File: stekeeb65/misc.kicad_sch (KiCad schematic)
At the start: 7 parts, among them J0 Conn_02x03_Odd_Even, J1 TYPE-C-31-M12_13_EDITED, U0 WE-TVS-82400102

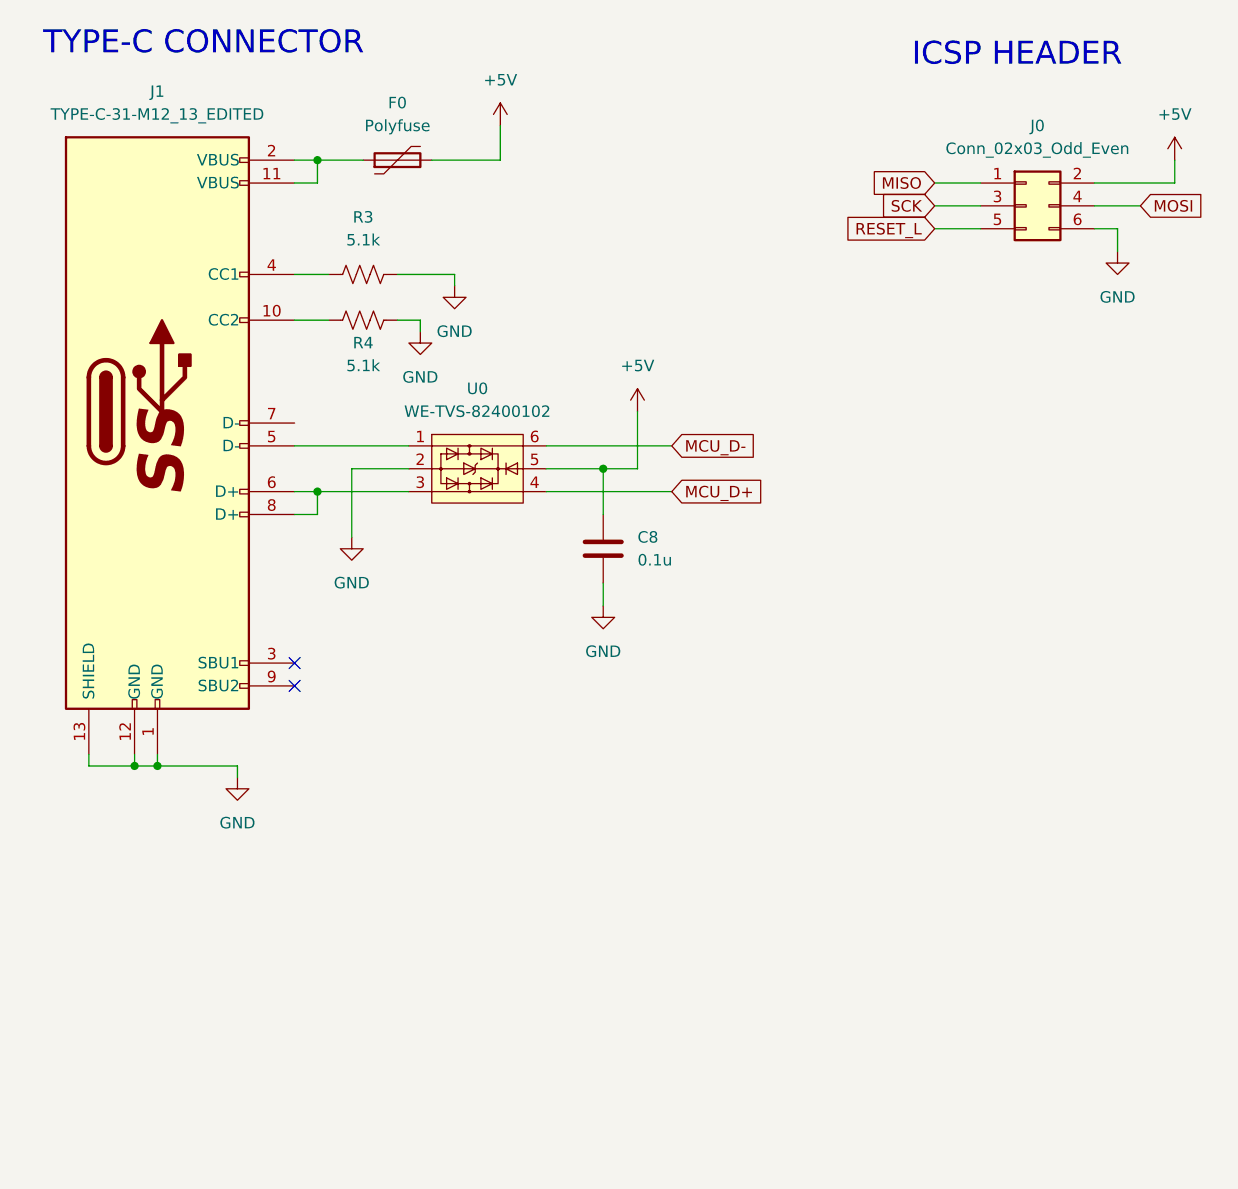
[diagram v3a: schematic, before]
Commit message: Started layout for keyboard. still need to verify LED driver schematic
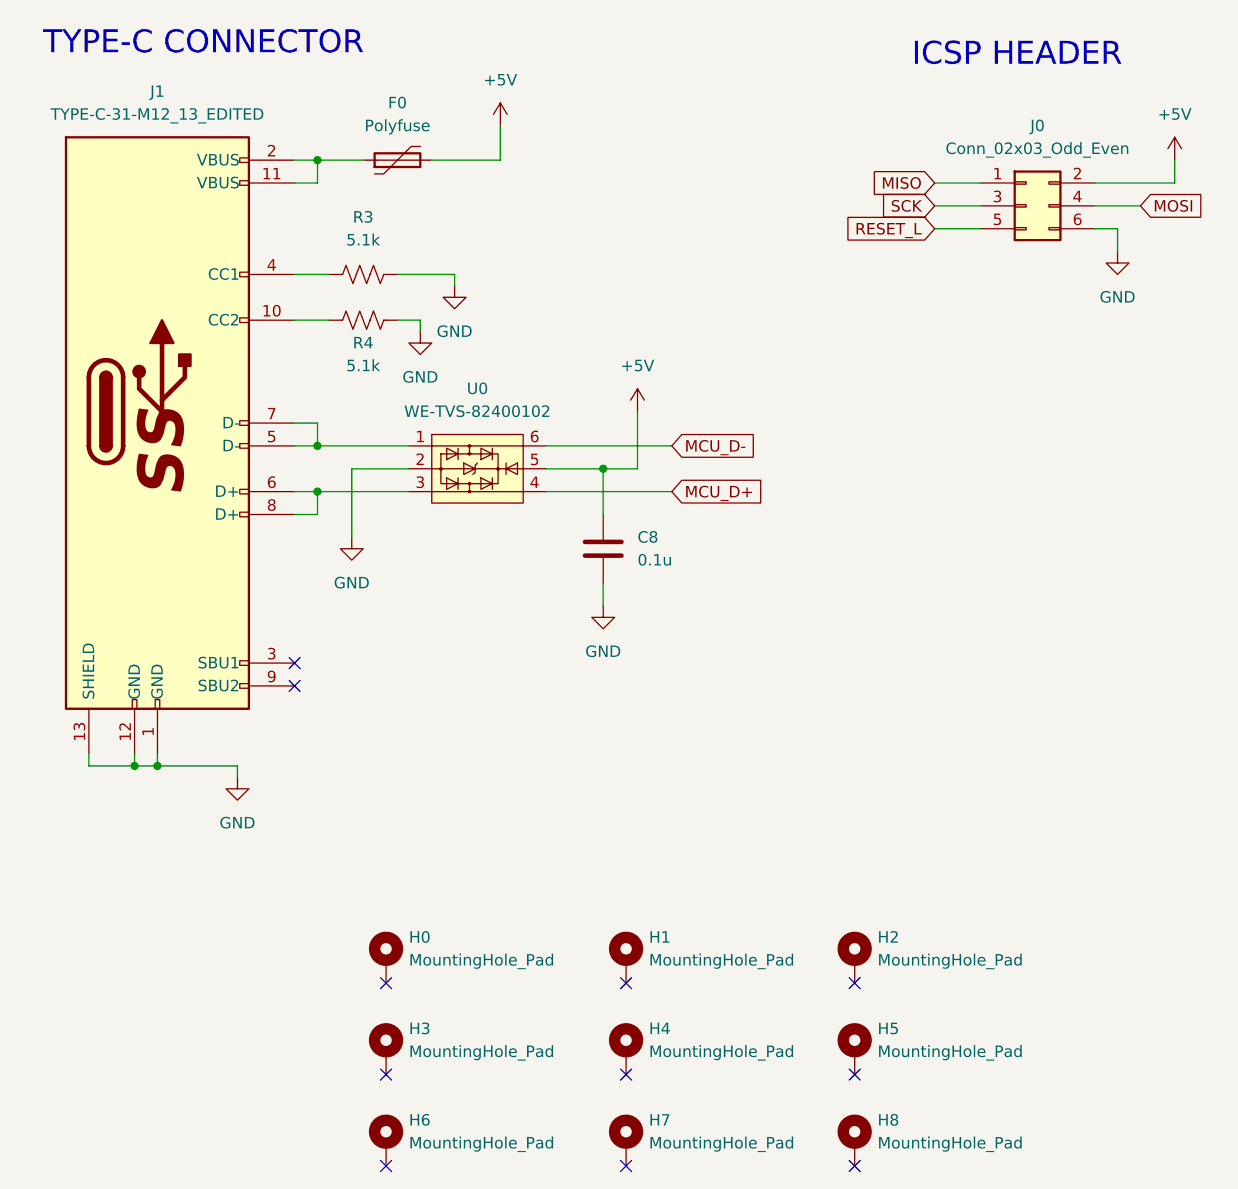
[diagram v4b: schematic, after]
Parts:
- added H0, H1, H2, H3, H4, H5, H6, H7, H8: MountingHole_Pad, MountingHole:MountingHole_2.2mm_M2_DIN965_Pad_TopOnly, symbol Mechanical:MountingHole_Pad
- C8: footprint Capacitor_SMD:C_0805_2012Metric_Pad1.18x1.45mm_HandSolder -> Capacitor_SMD:C_0603_1608Metric_Pad1.08x0.95mm_HandSolder
- J1: footprint Type-C:HRO-TYPE-C-31-M-12-HandSoldering -> Type-C:HRO-TYPE-C-31-M-12-Assembly
- R3, R4: footprint Resistor_SMD:R_0805_2012Metric_Pad1.20x1.40mm_HandSolder -> Resistor_SMD:R_0603_1608Metric_Pad0.98x0.95mm_HandSolder
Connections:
- net at J1.5 (D-), U0.1: now also J1.7 (D-)
- no-connect marks 2 -> 11
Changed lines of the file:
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@@
   (junction (at 57.15 71.12) (diameter 0) (color 0 0 0 0)
   )
+  (junction (at 57.15 66.04) (diameter 0) (color 0 0 0 0)
+  )
   (junction (at 88.9 68.58) (diameter 0) (color 0 0 0 0)
   )
@@
   (junction (at 57.15 34.29) (diameter 0) (color 0 0 0 0)
   )
+  (no_connect (at 91.44 135.89))
+  (no_connect (at 91.44 146.05))
+  (no_connect (at 116.84 135.89))
+  (no_connect (at 116.84 125.73))
+  (no_connect (at 64.77 125.73))
+  (no_connect (at 91.44 125.73))
+  (no_connect (at 64.77 146.05))
+  (no_connect (at 116.84 146.05))
   (no_connect (at 54.61 92.71))
   (no_connect (at 54.61 90.17))
+  (no_connect (at 64.77 135.89))
   (wire (pts (xy 31.75 101.6) (xy 31.75 100.33))
     (stroke (width 0) (type default) (color 0 0 0 0))
@@
     (stroke (width 0) (type default) (color 0 0 0 0))
   )
+  (wire (pts (xy 54.61 63.5) (xy 57.15 63.5))
+    (stroke (width 0) (type default) (color 0 0 0 0))
+  )
   (wire (pts (xy 66.04 46.99) (xy 72.39 46.99))
     (stroke (width 0) (type default) (color 0 0 0 0))
@@
     (stroke (width 0) (type default) (color 0 0 0 0))
   )
+  (wire (pts (xy 57.15 63.5) (xy 57.15 66.04))
+    (stroke (width 0) (type default) (color 0 0 0 0))
+  )
   (wire (pts (xy 146.05 41.91) (xy 146.05 44.45))
     (stroke (width 0) (type default) (color 0 0 0 0))
@@
     (stroke (width 0) (type default) (color 0 0 0 0))
   )
-  (wire (pts (xy 54.61 66.04) (xy 67.31 66.04))
+  (wire (pts (xy 54.61 66.04) (xy 57.15 66.04))
     (stroke (width 0) (type default) (color 0 0 0 0))
   )
   (wire (pts (xy 60.96 76.2) (xy 60.96 68.58))
+    (stroke (width 0) (type default) (color 0 0 0 0))
+  )
+  (wire (pts (xy 57.15 66.04) (xy 67.31 66.04))
     (stroke (width 0) (type default) (color 0 0 0 0))
   )
@@
     (pin "1")
   )
+  (symbol (lib_id "Mechanical:MountingHole_Pad") (at 116.84 133.35 0) (unit 1)
+    (in_bom yes) (on_board yes) (fields_autoplaced)
+    (property "Reference" "H5" (id 0) (at 119.38 130.8099 0)
+      (effects (font (size 1.27 1.27)) (justify left))
+    )
+    (property "Value" "MountingHole_Pad" (id 1) (at 119.38 133.3499 0)
+      (effects (font (size 1.27 1.27)) (justify left))
+    )
+    (property "Footprint" "MountingHole:MountingHole_2.2mm_M2_DIN965_Pad_TopOnly" (id 2) (at 116.84 133.35 0)
+      (effects (font (size 1.27 1.27)) hide)
+    )
+    (property "Datasheet" "~" (id 3) (at 116.84 133.35 0)
+      (effects (font (size 1.27 1.27)) hide)
+    )
+    (pin "1")
+  )
+  (symbol (lib_id "Mechanical:MountingHole_Pad") (at 64.77 123.19 0) (unit 1)
+    (in_bom yes) (on_board yes) (fields_autoplaced)
+    (property "Reference" "H0" (id 0) (at 67.31 120.6499 0)
+      (effects (font (size 1.27 1.27)) (justify left))
+    )
+    (property "Value" "MountingHole_Pad" (id 1) (at 67.31 123.1899 0)
+      (effects (font (size 1.27 1.27)) (justify left))
+    )
+    (property "Footprint" "MountingHole:MountingHole_2.2mm_M2_DIN965_Pad_TopOnly" (id 2) (at 64.77 123.19 0)
+      (effects (font (size 1.27 1.27)) hide)
+    )
+    (property "Datasheet" "~" (id 3) (at 64.77 123.19 0)
+      (effects (font (size 1.27 1.27)) hide)
+    )
+    (pin "1")
+  )
   (symbol (lib_id "Device:C") (at 88.9 77.47 0) (unit 1)
     (in_bom yes) (on_board yes) (fields_autoplaced)
@@
       (effects (font (size 1.27 1.27)) (justify left))
     )
-    (property "Footprint" "Capacitor_SMD:C_0805_2012Metric_Pad1.18x1.45mm_HandSolder" (id 2) (at 89.8652 81.28 0)
+    (property "Footprint" "Capacitor_SMD:C_0603_1608Metric_Pad1.08x0.95mm_HandSolder" (id 2) (at 89.8652 81.28 0)
       (effects (font (size 1.27 1.27)) hide)
     )
@@
     (property "Reference" "J1" (id 0) (at 39.37 26.67 0))
     (property "Value" "TYPE-C-31-M12_13_EDITED" (id 1) (at 39.37 29.21 0))
-    (property "Footprint" "Type-C:HRO-TYPE-C-31-M-12-HandSoldering" (id 2) (at 26.67 62.23 90)
+    (property "Footprint" "Type-C:HRO-TYPE-C-31-M-12-Assembly" (id 2) (at 26.67 62.23 90)
       (effects (font (size 1.27 1.27)) hide)
     )
@@
     (property "Reference" "R3" (id 0) (at 62.23 40.64 90))
     (property "Value" "5.1k" (id 1) (at 62.23 43.18 90))
-    (property "Footprint" "Resistor_SMD:R_0805_2012Metric_Pad1.20x1.40mm_HandSolder" (id 2) (at 62.484 45.974 90)
+    (property "Footprint" "Resistor_SMD:R_0603_1608Metric_Pad0.98x0.95mm_HandSolder" (id 2) (at 62.484 45.974 90)
       (effects (font (size 1.27 1.27)) hide)
     )
@@
     (pin "1")
     (pin "2")
+  )
+  (symbol (lib_id "Mechanical:MountingHole_Pad") (at 91.44 123.19 0) (unit 1)
+    (in_bom yes) (on_board yes) (fields_autoplaced)
+    (property "Reference" "H1" (id 0) (at 93.98 120.6499 0)
+      (effects (font (size 1.27 1.27)) (justify left))
+    )
+    (property "Value" "MountingHole_Pad" (id 1) (at 93.98 123.1899 0)
+      (effects (font (size 1.27 1.27)) (justify left))
+    )
+    (property "Footprint" "MountingHole:MountingHole_2.2mm_M2_DIN965_Pad_TopOnly" (id 2) (at 91.44 123.19 0)
+      (effects (font (size 1.27 1.27)) hide)
+    )
+    (property "Datasheet" "~" (id 3) (at 91.44 123.19 0)
+      (effects (font (size 1.27 1.27)) hide)
+    )
+    (pin "1")
   )
   (symbol (lib_id "power:+5V") (at 92.71 62.23 0) (unit 1)
@@
     (property "Reference" "R4" (id 0) (at 62.23 54.61 90))
     (property "Value" "5.1k" (id 1) (at 62.23 57.15 90))
-    (property "Footprint" "Resistor_SMD:R_0805_2012Metric_Pad1.20x1.40mm_HandSolder" (id 2) (at 62.484 51.054 90)
+    (property "Footprint" "Resistor_SMD:R_0603_1608Metric_Pad0.98x0.95mm_HandSolder" (id 2) (at 62.484 51.054 90)
       (effects (font (size 1.27 1.27)) hide)
     )
@@
     (pin "1")
   )
+  (symbol (lib_id "Mechanical:MountingHole_Pad") (at 91.44 133.35 0) (unit 1)
+    (in_bom yes) (on_board yes) (fields_autoplaced)
+    (property "Reference" "H4" (id 0) (at 93.98 130.8099 0)
+      (effects (font (size 1.27 1.27)) (justify left))
+    )
+    (property "Value" "MountingHole_Pad" (id 1) (at 93.98 133.3499 0)
+      (effects (font (size 1.27 1.27)) (justify left))
+    )
+    (property "Footprint" "MountingHole:MountingHole_2.2mm_M2_DIN965_Pad_TopOnly" (id 2) (at 91.44 133.35 0)
+      (effects (font (size 1.27 1.27)) hide)
+    )
+    (property "Datasheet" "~" (id 3) (at 91.44 133.35 0)
+      (effects (font (size 1.27 1.27)) hide)
+    )
+    (pin "1")
+  )
   (symbol (lib_id "power:+5V") (at 77.47 30.48 0) (unit 1)
     (in_bom yes) (on_board yes) (fields_autoplaced)
@@
       (effects (font (size 1.27 1.27)) hide)
     )
+    (pin "1")
+  )
+  (symbol (lib_id "Mechanical:MountingHole_Pad") (at 64.77 133.35 0) (unit 1)
+    (in_bom yes) (on_board yes) (fields_autoplaced)
+    (property "Reference" "H3" (id 0) (at 67.31 130.8099 0)
+      (effects (font (size 1.27 1.27)) (justify left))
+    )
+    (property "Value" "MountingHole_Pad" (id 1) (at 67.31 133.3499 0)
+      (effects (font (size 1.27 1.27)) (justify left))
+    )
+    (property "Footprint" "MountingHole:MountingHole_2.2mm_M2_DIN965_Pad_TopOnly" (id 2) (at 64.77 133.35 0)
+      (effects (font (size 1.27 1.27)) hide)
+    )
+    (property "Datasheet" "~" (id 3) (at 64.77 133.35 0)
+      (effects (font (size 1.27 1.27)) hide)
+    )
+    (pin "1")
+  )
+  (symbol (lib_id "Mechanical:MountingHole_Pad") (at 91.44 143.51 0) (unit 1)
+    (in_bom yes) (on_board yes) (fields_autoplaced)
+    (property "Reference" "H7" (id 0) (at 93.98 140.9699 0)
+      (effects (font (size 1.27 1.27)) (justify left))
+    )
+    (property "Value" "MountingHole_Pad" (id 1) (at 93.98 143.5099 0)
+      (effects (font (size 1.27 1.27)) (justify left))
+    )
+    (property "Footprint" "MountingHole:MountingHole_2.2mm_M2_DIN965_Pad_TopOnly" (id 2) (at 91.44 143.51 0)
+      (effects (font (size 1.27 1.27)) hide)
+    )
+    (property "Datasheet" "~" (id 3) (at 91.44 143.51 0)
+      (effects (font (size 1.27 1.27)) hide)
+    )
+    (pin "1")
+  )
+  (symbol (lib_id "Mechanical:MountingHole_Pad") (at 116.84 143.51 0) (unit 1)
+    (in_bom yes) (on_board yes) (fields_autoplaced)
+    (property "Reference" "H8" (id 0) (at 119.38 140.9699 0)
+      (effects (font (size 1.27 1.27)) (justify left))
+    )
+    (property "Value" "MountingHole_Pad" (id 1) (at 119.38 143.5099 0)
+      (effects (font (size 1.27 1.27)) (justify left))
+    )
+    (property "Footprint" "MountingHole:MountingHole_2.2mm_M2_DIN965_Pad_TopOnly" (id 2) (at 116.84 143.51 0)
+      (effects (font (size 1.27 1.27)) hide)
+    )
+    (property "Datasheet" "~" (id 3) (at 116.84 143.51 0)
+      (effects (font (size 1.27 1.27)) hide)
+    )
+    (pin "1")
+  )
+  (symbol (lib_id "Mechanical:MountingHole_Pad") (at 64.77 143.51 0) (unit 1)
+    (in_bom yes) (on_board yes) (fields_autoplaced)
+    (property "Reference" "H6" (id 0) (at 67.31 140.9699 0)
+      (effects (font (size 1.27 1.27)) (justify left))
+    )
+    (property "Value" "MountingHole_Pad" (id 1) (at 67.31 143.5099 0)
+      (effects (font (size 1.27 1.27)) (justify left))
+    )
+    (property "Footprint" "MountingHole:MountingHole_2.2mm_M2_DIN965_Pad_TopOnly" (id 2) (at 64.77 143.51 0)
+      (effects (font (size 1.27 1.27)) hide)
+    )
+    (property "Datasheet" "~" (id 3) (at 64.77 143.51 0)
+      (effects (font (size 1.27 1.27)) hide)
+    )
+    (pin "1")
+  )
+  (symbol (lib_id "Mechanical:MountingHole_Pad") (at 116.84 123.19 0) (unit 1)
+    (in_bom yes) (on_board yes) (fields_autoplaced)
+    (property "Reference" "H2" (id 0) (at 119.38 120.6499 0)
+      (effects (font (size 1.27 1.27)) (justify left))
+    )
+    (property "Value" "MountingHole_Pad" (id 1) (at 119.38 123.1899 0)
+      (effects (font (size 1.27 1.27)) (justify left))
+    )
+    (property "Footprint" "MountingHole:MountingHole_2.2mm_M2_DIN965_Pad_TopOnly" (id 2) (at 116.84 123.19 0)
+      (effects (font (size 1.27 1.27)) hide)
+    )
+    (property "Datasheet" "~" (id 3) (at 116.84 123.19 0)
+      (effects (font (size 1.27 1.27)) hide)
+    )
